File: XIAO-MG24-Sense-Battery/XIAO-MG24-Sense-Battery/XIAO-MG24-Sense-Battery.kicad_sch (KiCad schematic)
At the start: 9 parts, among them J1 Conn_01x02_Pin, J2 Conn_01x02_Pin, J5 Conn_01x02_Pin, SW1 SS12D00G3, U1 XIAO-MG24-Sense

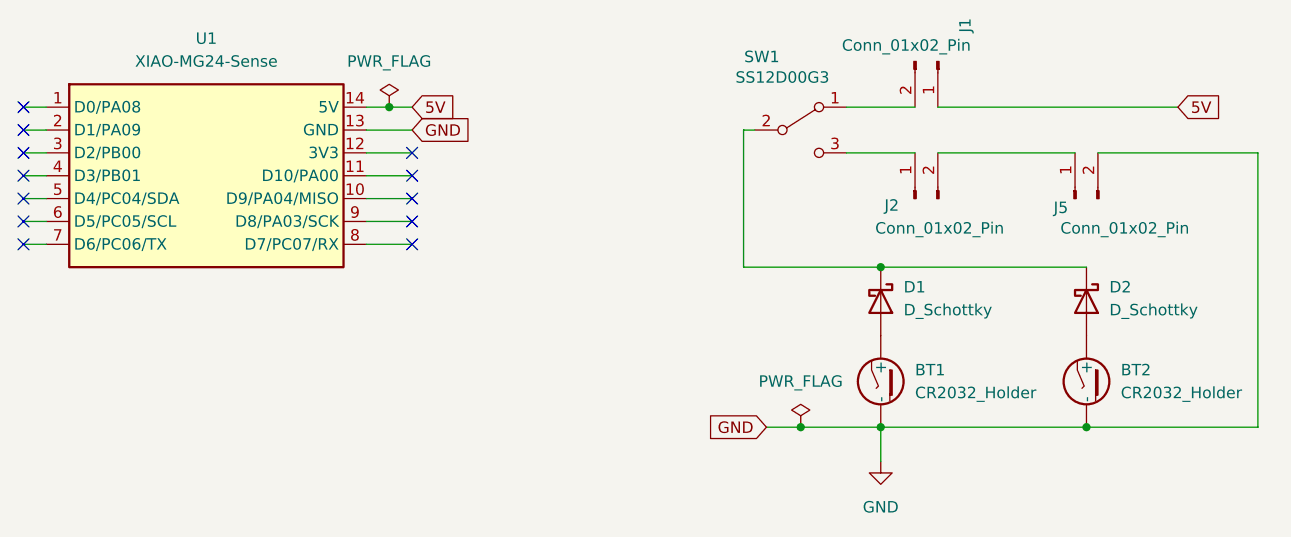
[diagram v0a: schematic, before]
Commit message: Modified PCB Data
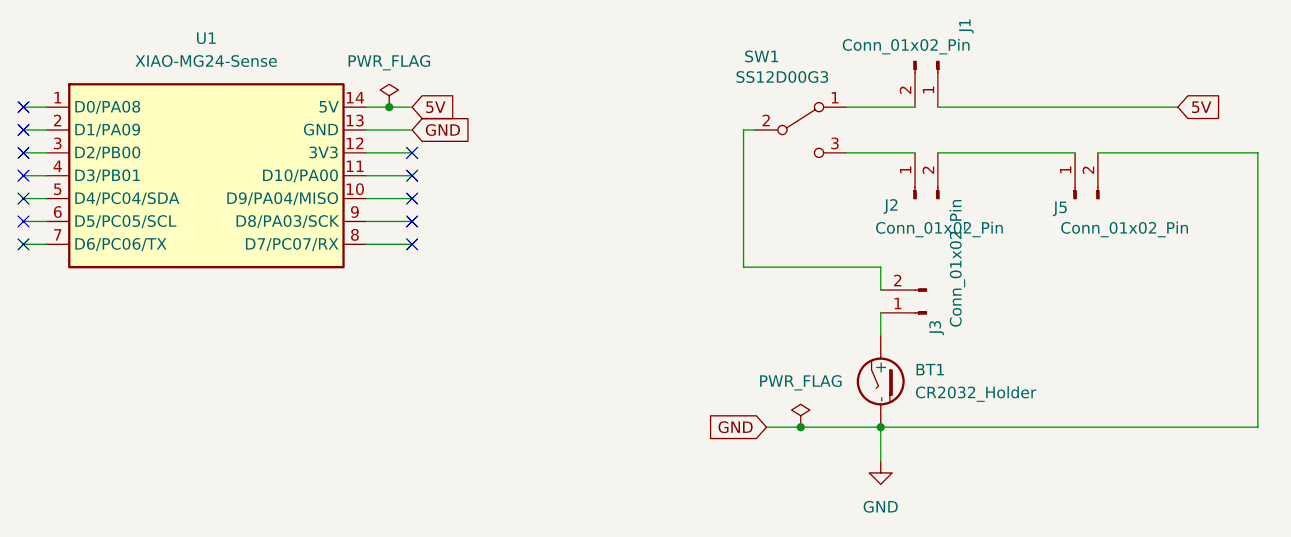
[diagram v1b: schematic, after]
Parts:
- removed BT2: CR2032_Holder, CR2032-holder:CR2032-Holder, symbol CR2032-Holder:CR2032_Holder
- removed D1, D2: D_Schottky, Diode_THT:D_DO-41_SOD81_P7.62mm_Horizontal, symbol Device:D_Schottky
- added J3: Conn_01x02_Pin, Connector_PinHeader_2.54mm:PinHeader_1x02_P2.54mm_Vertical, symbol Connector:Conn_01x02_Pin
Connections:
- net at SW1.2 (COM): now also J3.2 (Pin_2)
- net at BT1.1 (+): now also J3.1 (Pin_1)
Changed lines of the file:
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@@
-	)
-	(junction
-		(at 163.83 59.69)
-		(diameter 0)
-		(color 0 0 0 0)
-	)
-	(junction
-		(at 140.97 41.91)
-		(diameter 0)
-		(color 0 0 0 0)
 	)
 	(junction
@@
 	(wire
 		(pts
-			(xy 140.97 41.91) (xy 163.83 41.91)
-		)
-		(stroke
-			(width 0)
-			(type default)
-		)
-	)
-	(wire
-		(pts
 			(xy 83.82 26.67) (xy 88.9 26.67)
 		)
@@
 	(wire
 		(pts
-			(xy 163.83 59.69) (xy 140.97 59.69)
-		)
-		(stroke
-			(width 0)
-			(type default)
-		)
-	)
-	(wire
-		(pts
 			(xy 45.72 34.29) (xy 48.26 34.29)
 		)
@@
 	(wire
 		(pts
+			(xy 140.97 41.91) (xy 140.97 44.45)
+		)
+		(stroke
+			(width 0)
+			(type default)
+		)
+	)
+	(wire
+		(pts
 			(xy 83.82 36.83) (xy 88.9 36.83)
 		)
@@
 	(wire
 		(pts
+			(xy 140.97 46.99) (xy 140.97 49.53)
+		)
+		(stroke
+			(width 0)
+			(type default)
+		)
+	)
+	(wire
+		(pts
 			(xy 83.82 34.29) (xy 88.9 34.29)
 		)
@@
 	(wire
 		(pts
-			(xy 182.88 59.69) (xy 163.83 59.69)
+			(xy 140.97 59.69) (xy 182.88 59.69)
 		)
 		(stroke
@@
 				(justify left)
 				(hide yes)
+			)
+		)
+	)
+	(symbol
+		(lib_id "Connector:Conn_01x02_Pin")
+		(at 146.05 46.99 180)
+		(unit 1)
+		(exclude_from_sim no)
+		(in_bom yes)
+		(on_board yes)
+		(dnp no)
+		(property "Reference" "J3"
+			(at 147.066 47.752 90)
+			(effects
+				(font
+					(size 1.27 1.27)
+				)
+				(justify left)
+			)
+		)
+		(property "Value" "Conn_01x02_Pin"
+			(at 149.352 34.29 90)
+			(effects
+				(font
+					(size 1.27 1.27)
+				)
+				(justify left)
+			)
+		)
+		(property "Footprint" "Connector_PinHeader_2.54mm:PinHeader_1x02_P2.54mm_Vertical"
+			(at 146.05 46.99 0)
+			(effects
+				(font
+					(size 1.27 1.27)
+				)
+				(hide yes)
+			)
+		)
+		(property "Datasheet" "~"
+			(at 146.05 46.99 0)
+			(effects
+				(font
+					(size 1.27 1.27)
+				)
+				(hide yes)
+			)
+		)
+		(property "Description" "Generic connector, single row, 01x02, script generated"
+			(at 146.05 46.99 0)
+			(effects
+				(font
+					(size 1.27 1.27)
+				)
+				(hide yes)
+			)
+		)
+		(pin "1"
+		)
+		(pin "2"
+		)
+		(instances
+			(project "XIAO-MG24-Sense-Battery"
+				(path "/9ab561bf-7754-489b-b6e1-4fe35361b16e"
+					(reference "J3")
+					(unit 1)
+				)
 			)
 		)
@@
 				(path "/9ab561bf-7754-489b-b6e1-4fe35361b16e"
 					(reference "J2")
-					(unit 1)
-				)
-			)
-		)
-	)
-	(symbol
-		(lib_id "CR2032-Holder:CR2032_Holder")
-		(at 163.83 54.61 90)
-		(unit 1)
-		(exclude_from_sim no)
-		(in_bom yes)
-		(on_board yes)
-		(dnp no)
-		(fields_autoplaced yes)
-		(property "Reference" "BT2"
-			(at 167.64 53.3399 90)
-			(effects
-				(font
-					(size 1.27 1.27)
-				)
-				(justify right)
-			)
-		)
-		(property "Value" "CR2032_Holder"
-			(at 167.64 55.8799 90)
-			(effects
-				(font
-					(size 1.27 1.27)
-				)
-				(justify right)
-			)
-		)
-		(property "Footprint" "CR2032-holder:CR2032-Holder"
-			(at 163.83 54.61 0)
-			(effects
-				(font
-					(size 1.27 1.27)
-				)
-				(hide yes)
-			)
-		)
-		(property "Datasheet" "https://akizukidenshi.com/goodsaffix/CH25-2032LF.pdf"
-			(at 173.482 37.846 0)
-			(effects
-				(font
-					(size 1.27 1.27)
-				)
-				(hide yes)
-			)
-		)
-		(property "Description" "CR2032 Battery Holder, Akizuki 100706"
-			(at 170.688 46.228 0)
-			(effects
-				(font
-					(size 1.27 1.27)
-				)
-				(hide yes)
-			)
-		)
-		(pin "2"
-		)
-		(pin "1"
-		)
-		(instances
-			(project "XIAO-MG24-Sense-Battery"
-				(path "/9ab561bf-7754-489b-b6e1-4fe35361b16e"
-					(reference "BT2")
-					(unit 1)
-				)
-			)
-		)
-	)
-	(symbol
-		(lib_id "Device:D_Schottky")
-		(at 140.97 45.72 270)
-		(unit 1)
-		(exclude_from_sim no)
-		(in_bom yes)
-		(on_board yes)
-		(dnp no)
-		(fields_autoplaced yes)
-		(property "Reference" "D1"
-			(at 143.51 44.1324 90)
-			(effects
-				(font
-					(size 1.27 1.27)
-				)
-				(justify left)
-			)
-		)
-		(property "Value" "D_Schottky"
-			(at 143.51 46.6724 90)
-			(effects
-				(font
-					(size 1.27 1.27)
-				)
-				(justify left)
-			)
-		)
-		(property "Footprint" "Diode_THT:D_DO-41_SOD81_P7.62mm_Horizontal"
-			(at 140.97 45.72 0)
-			(effects
-				(font
-					(size 1.27 1.27)
-				)
-				(hide yes)
-			)
-		)
-		(property "Datasheet" "~"
-			(at 140.97 45.72 0)
-			(effects
-				(font
-					(size 1.27 1.27)
-				)
-				(hide yes)
-			)
-		)
-		(property "Description" "Schottky diode"
-			(at 140.97 45.72 0)
-			(effects
-				(font
-					(size 1.27 1.27)
-				)
-				(hide yes)
-			)
-		)
-		(pin "2"
-		)
-		(pin "1"
-		)
-		(instances
-			(project ""
-				(path "/9ab561bf-7754-489b-b6e1-4fe35361b16e"
-					(reference "D1")
 					(unit 1)
 				)
@@
 					(unit 1)
 				)
-			)
-		)
-	)
-	(symbol
-		(lib_id "Device:D_Schottky")
-		(at 163.83 45.72 270)
-		(unit 1)
-		(exclude_from_sim no)
-		(in_bom yes)
-		(on_board yes)
-		(dnp no)
-		(fields_autoplaced yes)
-		(property "Reference" "D2"
-			(at 166.37 44.1324 90)
-			(effects
-				(font
-					(size 1.27 1.27)
-				)
-				(justify left)
-			)
-		)
-		(property "Value" "D_Schottky"
-			(at 166.37 46.6724 90)
-			(effects
-				(font
-					(size 1.27 1.27)
-				)
-				(justify left)
-			)
-		)
-		(property "Footprint" "Diode_THT:D_DO-41_SOD81_P7.62mm_Horizontal"
-			(at 163.83 45.72 0)
-			(effects
-				(font
-					(size 1.27 1.27)
-				)
-				(hide yes)
-			)
-		)
-		(property "Datasheet" "~"
-			(at 163.83 45.72 0)
-			(effects
-				(font
-					(size 1.27 1.27)
-				)
-				(hide yes)
-			)
-		)
-		(property "Description" "Schottky diode"
-			(at 163.83 45.72 0)
-			(effects
-				(font
-					(size 1.27 1.27)
-				)
-				(hide yes)
-			)
-		)
-		(pin "2"
-		)
-		(pin "1"
-		)
-		(instances
-			(project "XIAO-MG24-Sense-Battery"
-				(path "/9ab561bf-7754-489b-b6e1-4fe35361b16e"
-					(reference "D2")
-					(unit 1)
-				)
